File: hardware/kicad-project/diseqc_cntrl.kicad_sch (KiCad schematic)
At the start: 19 parts, among them IC1 TPS560200DBVR, J1 Barrel Jack

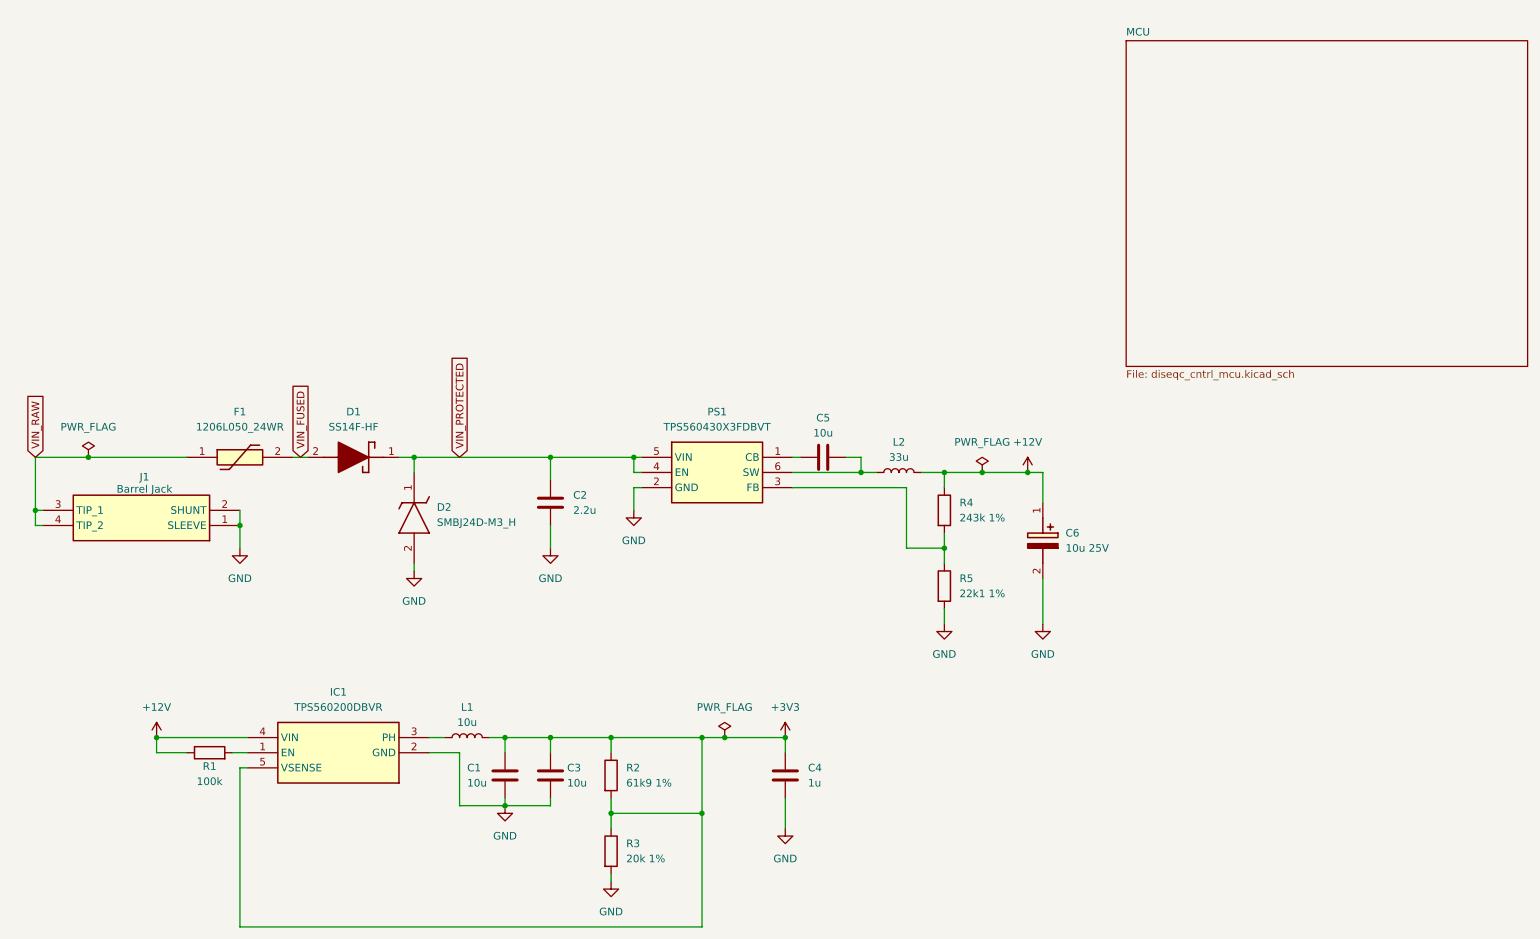
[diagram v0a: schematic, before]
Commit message: Corrective changes to power regulation: F1, PS1
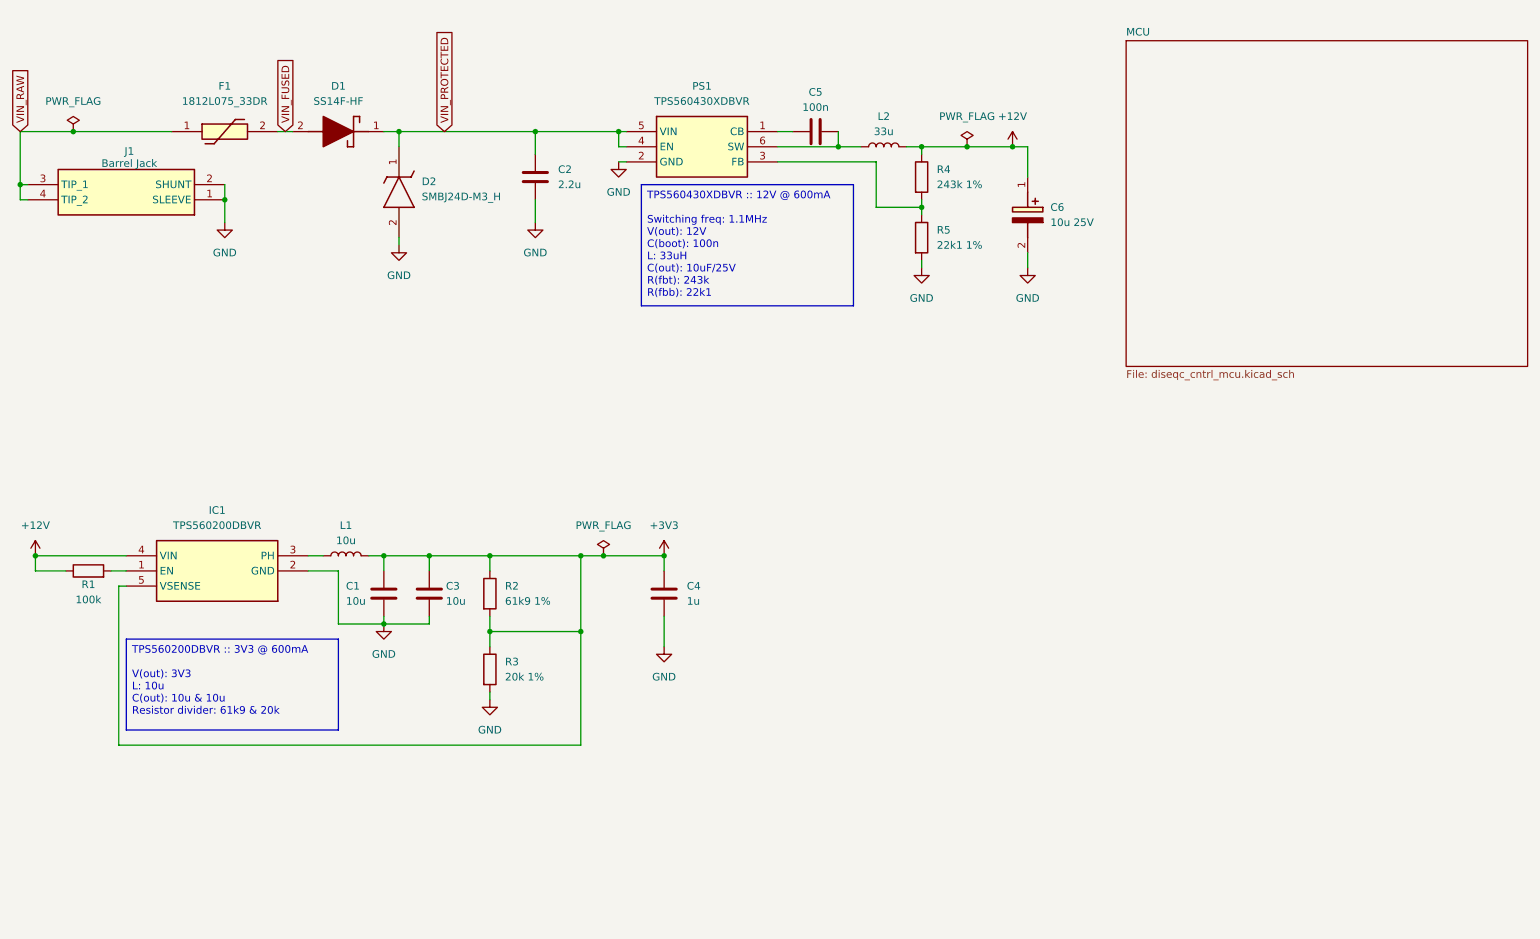
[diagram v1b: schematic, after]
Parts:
- C5: value 10u -> 100n
- C6: footprint LIB_865080440002:CAPAE400X550N -> diseqc_cntrl:CAPAE400X550N
- D1: footprint LIB_SS14_HF:SODFL4626X120N -> diseqc_cntrl:SODFL4626X120N
- D2: footprint LIB_SMBJ24D-M3_H:DIOM5436X244N -> diseqc_cntrl:DIOM5436X244N
- F1: value 1206L050_24WR -> 1812L075_33DR; footprint LIB_1206L050_24WR:1206L075132WR -> diseqc_cntrl:1812L010DR; symbol diseqc_cntrl:1206L050_24WR -> 1812L075_33DR:1812L075_33DR; Manufacturer_Part_Number 1206L050/24WR -> 1812L075/33DR; Mouser Part Number 576-1206L050/24WR -> 576-1812L075/33DR; Mouser Price/Stock https://www.mouser.co.uk/ProductDetail/Littelfuse/1206L050-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 -> https://www.mouser.co.uk/ProductDetail/Littelfuse/1812L075-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
- IC1: footprint LIB_TPS560200DBVR:SOT95P280X145-5N -> diseqc_cntrl:SOT95P280X145-5N
- J1: footprint LIB_RASM742TRX:RASM742TRX -> diseqc_cntrl:RASM742TRX; My Stock 0 -> (none)
- L2: footprint LIB_74404032330:INDPM3030X150N -> diseqc_cntrl:INDPM3030X150N; My Stock 0 -> (none)
- PS1: value TPS560430X3FDBVT -> TPS560430XDBVR; footprint SOT95P280X145-6N -> diseqc_cntrl:SOT95P280X145-6N; symbol diseqc_cntrl:TPS560430X3FDBVT -> tps5604:TPS560430XDBVR; Manufacturer_Part_Number TPS560430X3FDBVT -> TPS560430XDBVR; Mouser Part Number 595-TPS560430X3FDBVT -> 595-TPS560430XDBVR; Mouser Price/Stock https://www.mouser.co.uk/ProductDetail/Texas-Instruments/TPS560430X3FDBVT?qs=y6ZabgHbY%252BwVnm98XeNv8w%3D%3D -> https://www.mouser.co.uk/ProductDetail/Texas-Instruments/TPS560430XDBVR?qs=%252BEew9%252B0nqrDFUDwUxL0Ntw%3D%3D
- R1: My Stock 50 -> (none)
- R2, R3, R4, R5: My Stock 0 -> (none)
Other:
- moved on the sheet: C1, C2, C3, C4, C5, C6, D1, D2, F1, IC1, J1, L1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

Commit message: Added test points for power regulation
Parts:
- added TP1, TP2, TP3: TestPoint, TestPoint:TestPoint_THTPad_D1.0mm_Drill0.5mm, symbol Connector:TestPoint
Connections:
- net +12V: now also TP2.1
- net +3V3: now also TP3.1
- net VIN_FUSED: now also TP1.1
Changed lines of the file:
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@@
+	)
+	(junction
+		(at 62.23 39.37)
+		(diameter 0)
+		(color 0 0 0 0)
 	)
 	(junction
@@
 	(wire
 		(pts
-			(xy 60.96 39.37) (xy 63.5 39.37)
+			(xy 60.96 39.37) (xy 62.23 39.37)
 		)
 		(stroke
@@
 	(wire
 		(pts
+			(xy 86.36 104.14) (xy 86.36 110.49)
+		)
+		(stroke
+			(width 0)
+			(type default)
+		)
+	)
+	(wire
+		(pts
+			(xy 168.91 33.02) (xy 168.91 41.91)
+		)
+		(stroke
+			(width 0)
+			(type default)
+		)
+	)
+	(wire
+		(pts
 			(xy 17.78 48.26) (xy 17.78 39.37)
 		)
@@
 		(pts
 			(xy 35.56 115.57) (xy 34.29 115.57)
+		)
+		(stroke
+			(width 0)
+			(type default)
+		)
+	)
+	(wire
+		(pts
+			(xy 62.23 39.37) (xy 63.5 39.37)
 		)
 		(stroke
@@
 	)
 	(symbol
+		(lib_id "Connector:TestPoint")
+		(at 62.23 39.37 180)
+		(unit 1)
+		(exclude_from_sim no)
+		(in_bom yes)
+		(on_board yes)
+		(dnp no)
+		(fields_autoplaced yes)
+		(property "Reference" "TP1"
+			(at 64.77 41.4019 0)
+			(effects
+				(font
+					(size 1.27 1.27)
+				)
+				(justify right)
+			)
+		)
+		(property "Value" "TestPoint"
+			(at 64.77 43.9419 0)
+			(effects
+				(font
+					(size 1.27 1.27)
+				)
+				(justify right)
+			)
+		)
+		(property "Footprint" "TestPoint:TestPoint_THTPad_D1.0mm_Drill0.5mm"
+			(at 57.15 39.37 0)
+			(effects
+				(font
+					(size 1.27 1.27)
+				)
+				(hide yes)
+			)
+		)
+		(property "Datasheet" "~"
+			(at 57.15 39.37 0)
+			(effects
+				(font
+					(size 1.27 1.27)
+				)
+				(hide yes)
+			)
+		)
+		(property "Description" "test point"
+			(at 62.23 39.37 0)
+			(effects
+				(font
+					(size 1.27 1.27)
+				)
+				(hide yes)
+			)
+		)
+		(pin "1"
+		)
+		(instances
+			(project "diseqc_cntrl"
+				(path "/82a905d8-f1d7-4995-9c16-94cf3cdcaad9"
+					(reference "TP1")
+					(unit 1)
+				)
+			)
+		)
+	)
+	(symbol
 		(lib_id "diseqc_cntrl:SMBJ24D-M3_H")
 		(at 81.28 41.91 270)
@@
 	)
 	(symbol
+		(lib_id "Connector:TestPoint")
+		(at 86.36 104.14 0)
+		(unit 1)
+		(exclude_from_sim no)
+		(in_bom yes)
+		(on_board yes)
+		(dnp no)
+		(fields_autoplaced yes)
+		(property "Reference" "TP3"
+			(at 88.9 99.5679 0)
+			(effects
+				(font
+					(size 1.27 1.27)
+				)
+				(justify left)
+			)
+		)
+		(property "Value" "TestPoint"
+			(at 88.9 102.1079 0)
+			(effects
+				(font
+					(size 1.27 1.27)
+				)
+				(justify left)
+			)
+		)
+		(property "Footprint" "TestPoint:TestPoint_THTPad_D1.0mm_Drill0.5mm"
+			(at 91.44 104.14 0)
+			(effects
+				(font
+					(size 1.27 1.27)
+				)
+				(hide yes)
+			)
+		)
+		(property "Datasheet" "~"
+			(at 91.44 104.14 0)
+			(effects
+				(font
+					(size 1.27 1.27)
+				)
+				(hide yes)
+			)
+		)
+		(property "Description" "test point"
+			(at 86.36 104.14 0)
+			(effects
+				(font
+					(size 1.27 1.27)
+				)
+				(hide yes)
+			)
+		)
+		(pin "1"
+		)
+		(instances
+			(project "diseqc_cntrl"
+				(path "/82a905d8-f1d7-4995-9c16-94cf3cdcaad9"
+					(reference "TP3")
+					(unit 1)
+				)
+			)
+		)
+	)
+	(symbol
 		(lib_id "diseqc_cntrl:GND")
 		(at 168.91 62.23 0)
@@
 					(unit 1)
 				)
+			)
+		)
+	)
+	(symbol
+		(lib_id "Connector:TestPoint")
+		(at 168.91 33.02 0)
+		(unit 1)
+		(exclude_from_sim no)
+		(in_bom yes)
+		(on_board yes)
+		(dnp no)
+		(fields_autoplaced yes)
+		(property "Reference" "TP2"
+			(at 171.45 28.4479 0)
+			(effects
+				(font
+					(size 1.27 1.27)
+				)
+				(justify left)
+			)
+		)
+		(property "Value" "TestPoint"
+			(at 171.45 30.9879 0)
+			(effects
+				(font
+					(size 1.27 1.27)
+				)
+				(justify left)
+			)
+		)
+		(property "Footprint" "TestPoint:TestPoint_THTPad_D1.0mm_Drill0.5mm"
+			(at 173.99 33.02 0)
+			(effects
+				(font
+					(size 1.27 1.27)
+				)
+				(hide yes)
+			)
+		)
+		(property "Datasheet" "~"
+			(at 173.99 33.02 0)
+			(effects
+				(font
+					(size 1.27 1.27)
+				)
+				(hide yes)
+			)
+		)
+		(property "Description" "test point"
+			(at 168.91 33.02 0)
+			(effects
+				(font
+					(size 1.27 1.27)
+				)
+				(hide yes)
+			)
+		)
+		(pin "1"
+		)
+		(instances
+			(project "diseqc_cntrl"
+				(path "/82a905d8-f1d7-4995-9c16-94cf3cdcaad9"
+					(reference "TP2")
+					(unit 1)
+				)

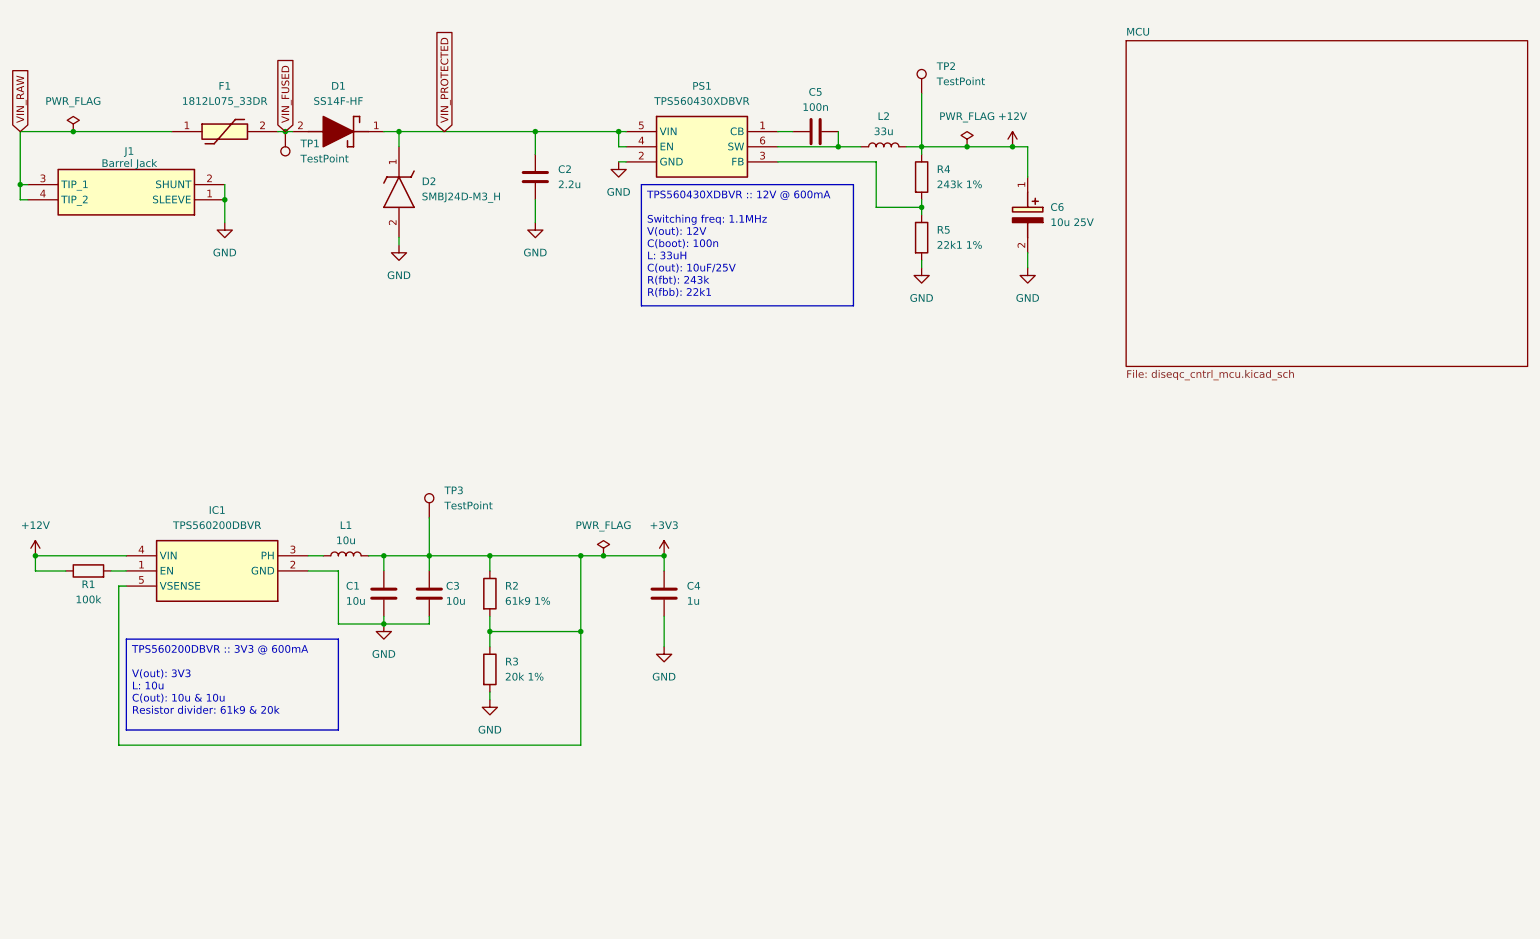
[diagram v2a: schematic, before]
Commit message: Added more test points
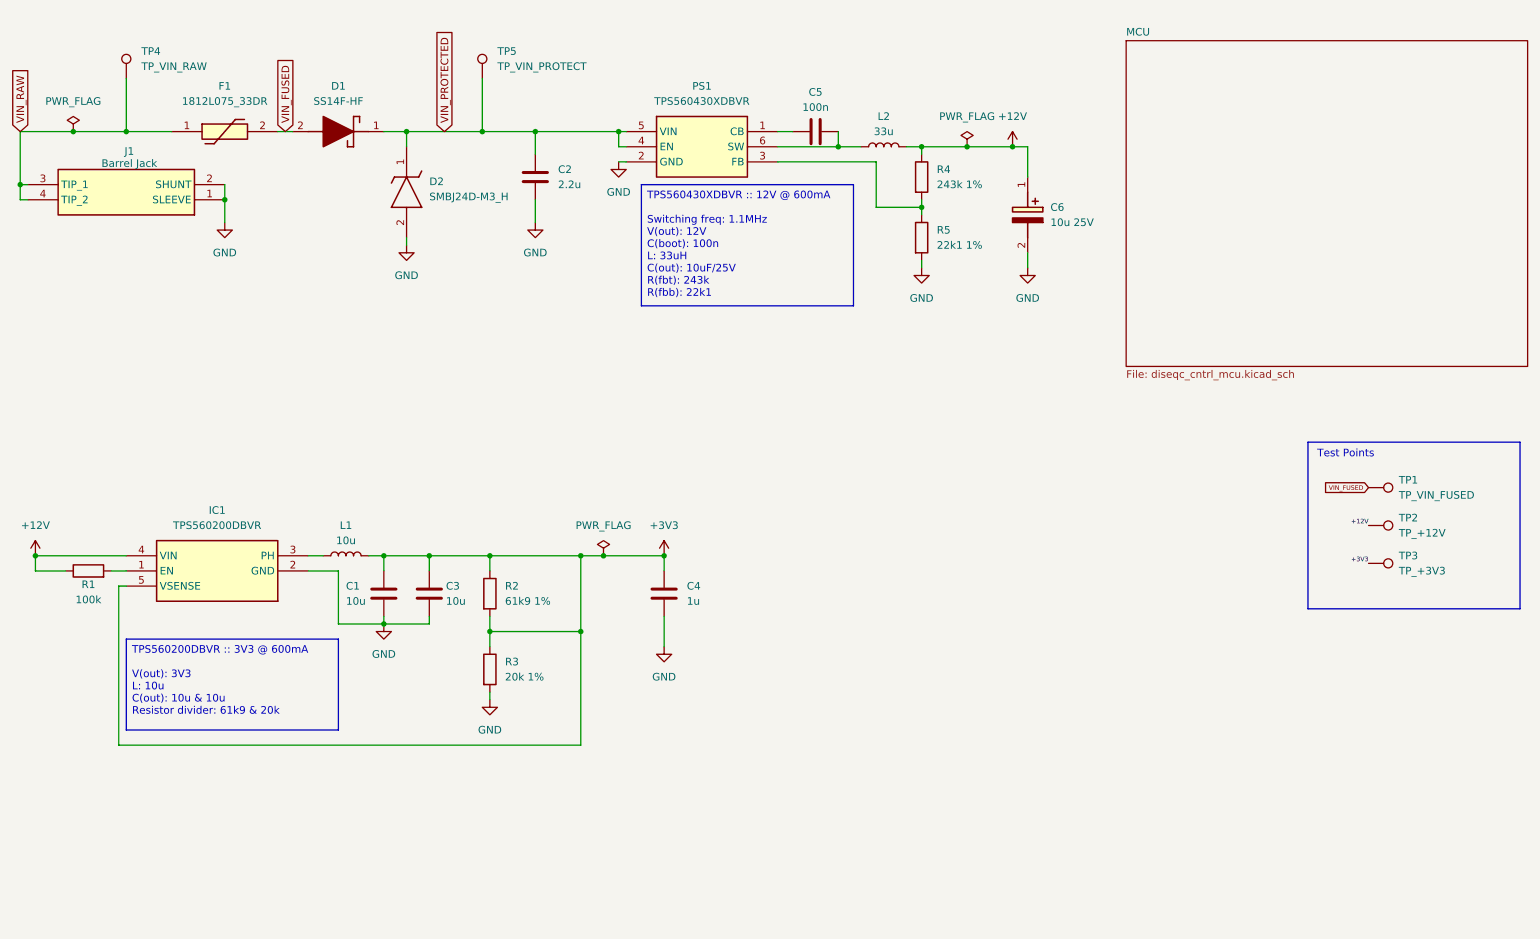
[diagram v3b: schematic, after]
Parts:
- added TP4: TP_VIN_RAW, TestPoint:TestPoint_THTPad_D1.0mm_Drill0.5mm, symbol Connector:TestPoint
- added TP5: TP_VIN_PROTECT, TestPoint:TestPoint_THTPad_D1.0mm_Drill0.5mm, symbol Connector:TestPoint
- TP1: value TestPoint -> TP_VIN_FUSED
- TP2: value TestPoint -> TP_+12V
- TP3: value TestPoint -> TP_+3V3
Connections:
- net VIN_PROTECTED: now also TP5.1
- net VIN_RAW: now also TP4.1
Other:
- note added: "Test Points"
- moved on the sheet: D2, TP1, TP2, TP3
